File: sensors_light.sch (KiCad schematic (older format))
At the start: 6 parts

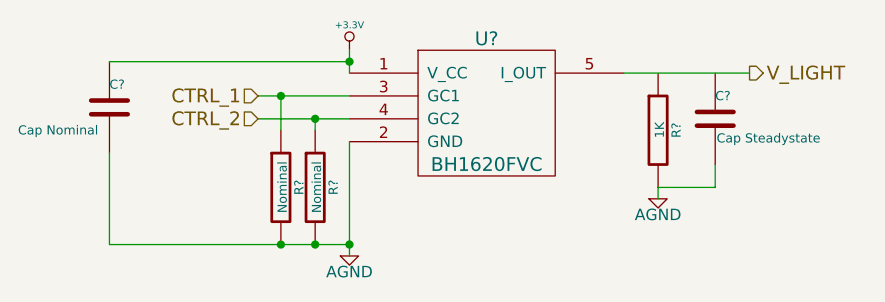
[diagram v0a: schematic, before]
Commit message: various fixes due to issues found in ERC
learned how to use invisible pins
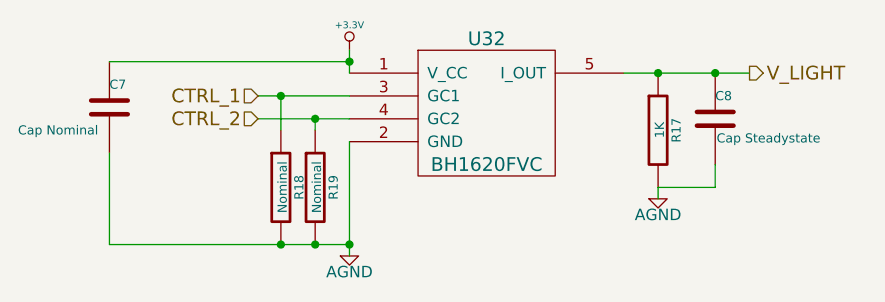
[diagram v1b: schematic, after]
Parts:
- gave numbers to parts that had none: 6
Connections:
- net V_LIGHT: now also C8.1, R17.1
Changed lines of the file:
@@
 Sheet 8 18
 Title ""
-Date "18 dec 2013"
+Date "20 dec 2013"
 Rev ""
 Comp ""
@@
 $EndDescr
 $Comp
-L R R?
+L R R18
 U 1 1 527B1EF8
 P 2650 1300
-F 0 "R?" V 2730 1300 40  0000 C CNN
+F 0 "R18" V 2730 1300 40  0000 C CNN
 F 1 "Nominal" V 2657 1301 40  0000 C CNN
 F 2 "~" V 2580 1300 30  0000 C CNN
@@
 $EndComp
 $Comp
-L R R?
+L R R17
 U 1 1 527B1F07
 P 4300 1050
-F 0 "R?" V 4380 1050 40  0000 C CNN
+F 0 "R17" V 4380 1050 40  0000 C CNN
 F 1 "1K" V 4307 1051 40  0000 C CNN
 F 2 "~" V 4230 1050 30  0000 C CNN
@@
 $EndComp
 $Comp
-L C C?
+L C C7
 U 1 1 527B1FD5
 P 1900 950
-F 0 "C?" H 1900 1050 40  0000 L CNN
+F 0 "C7" H 1900 1050 40  0000 L CNN
 F 1 "Cap Nominal" H 1500 850 40  0000 L CNN
 F 2 "~" H 1938 800 30  0000 C CNN
@@
 $EndComp
 $Comp
-L C C?
+L C C8
 U 1 1 527B20AA
 P 4550 1000
-F 0 "C?" H 4550 1100 40  0000 L CNN
+F 0 "C8" H 4550 1100 40  0000 L CNN
 F 1 "Cap Steadystate" H 4556 915 40  0000 L CNN
 F 2 "~" H 4588 850 30  0000 C CNN
@@
 $EndComp
 $Comp
-L R R?
+L R R19
 U 1 1 527B20B2
 P 2800 1300
-F 0 "R?" V 2880 1300 40  0000 C CNN
+F 0 "R19" V 2880 1300 40  0000 C CNN
 F 1 "Nominal" V 2807 1301 40  0000 C CNN
 F 2 "~" V 2730 1300 30  0000 C CNN
@@
 V_LIGHT
 $Comp
-L AGND #PWR?
+L AGND #PWR042
 U 1 1 527B22B7
 P 2950 1600
-F 0 "#PWR?" H 2950 1600 40  0001 C CNN
+F 0 "#PWR042" H 2950 1600 40  0001 C CNN
 F 1 "AGND" H 2950 1530 50  0000 C CNN
 F 2 "" H 2950 1600 60  0000 C CNN
@@
 $EndComp
 $Comp
-L AGND #PWR?
+L AGND #PWR043
 U 1 1 527B22C6
 P 4300 1350
-F 0 "#PWR?" H 4300 1350 40  0001 C CNN
+F 0 "#PWR043" H 4300 1350 40  0001 C CNN
 F 1 "AGND" H 4300 1280 50  0000 C CNN
 F 2 "" H 4300 1350 60  0000 C CNN
@@
 $EndComp
 $Comp
-L +3.3V #PWR?
+L +3.3V #PWR044
 U 1 1 527B22E1
 P 2950 700
-F 0 "#PWR?" H 2950 660 30  0001 C CNN
+F 0 "#PWR044" H 2950 660 30  0001 C CNN
 F 1 "+3.3V" H 2950 810 30  0000 C CNN
 F 2 "" H 2950 700 60  0000 C CNN
@@
 	4150 800  4700 800
 Wire Wire Line
-	2950 1100 2950 1550
+	2950 1100 2950 1600
 Wire Wire Line
-	2950 1550 2950 1600
-Wire Wire Line
-	2950 700  2950 750
-Wire Wire Line
-	2950 750  2950 800
+	2950 700  2950 800
 Wire Wire Line
 	4300 1300 4300 1350
@@
 Connection ~ 2950 750
 Wire Wire Line
-	2550 900  2650 900
+	2550 900  2950 900
 Wire Wire Line
-	2650 900  2950 900
-Wire Wire Line
-	2550 1000 2800 1000
-Wire Wire Line
-	2800 1000 2950 1000
+	2550 1000 2950 1000
 Wire Wire Line
 	2650 1050 2650 900
@@
 Connection ~ 2800 1000
 Wire Wire Line
-	1900 1550 2650 1550
-Wire Wire Line
-	2650 1550 2800 1550
-Wire Wire Line
-	2800 1550 2950 1550
+	1900 1550 2950 1550
 Connection ~ 2950 1550
 Connection ~ 2800 1550
@@
 	4550 1300 4550 1200
 $Comp
-L BH1620FVC U?
+L BH1620FVC U32
 U 1 1 529265A6
 P 3550 650
-F 0 "U?" H 3550 650 60  0000 C CNN
+F 0 "U32" H 3550 650 60  0000 C CNN
 F 1 "BH1620FVC" H 3550 100 60  0000 C CNN
 F 2 "~" H 3250 1050 60  0000 C CNN
@@
 	1    0    0    -1
 $EndComp
+Connection ~ 4300 800
+Connection ~ 4550 800
 $EndSCHEMATC

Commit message: placed components ... quite the task!
there is a lot of shit going on in this board... :D
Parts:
- renumbered C7 to C4, C8 to C5, U32 to U31
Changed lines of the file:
@@
 $Descr A4 11693 8268
 encoding utf-8
-Sheet 8 18
+Sheet 8 15
 Title ""
-Date "12 jan 2014"
+Date "18 jan 2014"
 Rev ""
 Comp ""
@@
 $EndComp
 $Comp
-L C C7
+L C C4
 U 1 1 527B1FD5
 P 1900 950
-F 0 "C7" H 1900 1050 40  0000 L CNN
+F 0 "C4" H 1900 1050 40  0000 L CNN
 F 1 "Cap Nominal" H 1500 850 40  0000 L CNN
 F 2 "~" H 1938 800 30  0000 C CNN
@@
 $EndComp
 $Comp
-L C C8
+L C C5
 U 1 1 527B20AA
 P 4550 1000
-F 0 "C8" H 4550 1100 40  0000 L CNN
+F 0 "C5" H 4550 1100 40  0000 L CNN
 F 1 "Cap Steadystate" H 4556 915 40  0000 L CNN
 F 2 "~" H 4588 850 30  0000 C CNN
@@
 V_LIGHT
 $Comp
-L AGND #PWR042
+L AGND #PWR037
 U 1 1 527B22B7
 P 2950 1600
-F 0 "#PWR042" H 2950 1600 40  0001 C CNN
+F 0 "#PWR037" H 2950 1600 40  0001 C CNN
 F 1 "AGND" H 2950 1530 50  0000 C CNN
 F 2 "" H 2950 1600 60  0000 C CNN
@@
 $EndComp
 $Comp
-L AGND #PWR043
+L AGND #PWR038
 U 1 1 527B22C6
 P 4300 1350
-F 0 "#PWR043" H 4300 1350 40  0001 C CNN
+F 0 "#PWR038" H 4300 1350 40  0001 C CNN
 F 1 "AGND" H 4300 1280 50  0000 C CNN
 F 2 "" H 4300 1350 60  0000 C CNN
@@
 $EndComp
 $Comp
-L +3.3V #PWR044
+L +3.3V #PWR039
 U 1 1 527B22E1
 P 2950 700
-F 0 "#PWR044" H 2950 660 30  0001 C CNN
+F 0 "#PWR039" H 2950 660 30  0001 C CNN
 F 1 "+3.3V" H 2950 810 30  0000 C CNN
 F 2 "" H 2950 700 60  0000 C CNN
@@
 	4550 1300 4550 1200
 $Comp
-L BH1620FVC U32
+L BH1620FVC U31
 U 1 1 529265A6
 P 3550 650
-F 0 "U32" H 3550 650 60  0000 C CNN
+F 0 "U31" H 3550 650 60  0000 C CNN
 F 1 "BH1620FVC" H 3550 100 60  0000 C CNN
 F 2 "~" H 3250 1050 60  0000 C CNN
